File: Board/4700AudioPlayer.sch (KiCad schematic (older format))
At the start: 24 parts, among them U10 74HC74, U11 74HC04, U14 74LS157, U5 74HC40103, U6 74HC40103, U7 74HC40103, U8 74HC40103

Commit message: [RAM] Added new parallel RAM ICs
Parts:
- removed U? (x2): 74HC04, symbol 74xx:74HC04
- removed U?: 74LS10, symbol 74xx:74LS08
- added U? (x2): CY62256-70PC, Package_DIP:DIP-28_W15.24mm, symbol Memory_RAM:CY62256-70PC
- added U? (x8): 74LS393, symbol 74xx:74LS393
- added U?: 74LS157, symbol 74xx:74LS157
- U? (x2): value 74LS10 -> 74LS08
- renumbered U14 to U?
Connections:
- net labels added: ramA_out0, ramA_out1, ramA_out2, ramA_out3, ramA_out4, ramA_out5, ramA_out6, ramA_out7, ramB_out0, ramB_out1, ramB_out2, ramB_out3, ramB_out4, ramB_out5, ramB_out6, ramB_out7
- net labels removed: byte_request, ram_init_cs
- wire segments 347 -> 473
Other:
- moved on the sheet: U11B, U?, U?B

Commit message: [Wave] Added module for played seconds and progress bar. Partially added module for total seconds.
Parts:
- removed U?: 74HC74, symbol 74xx:74HC74
- removed U?: 74HC590, symbol 74xx:74HC590
- added U? (x7): 74HC40103, Package_SO:SOIC-16_3.9x9.9mm_P1.27mm, symbol My_74xx:74HC40103
- added U? (x2): 74LS27, symbol 74xx:74LS27
- added U? (x10): 74LS393, symbol 74xx:74LS393
- added U? (x6): 74LS32, symbol 74xx:74LS32
- added U? (x6): 74LS85, symbol 74xx:74LS85
- added U? (x8): 74HC4511, symbol 74xx:74LS46
- added U?: 74LS154, symbol 74xx:74LS154
- renumbered U to U?
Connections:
- net labels added: reset, sec_clk, sys_clk, total_samples0, total_samples1, total_samples10, total_samples11, total_samples12, total_samples13, total_samples14, total_samples15, total_samples16, total_samples17, total_samples18, total_samples19, total_samples2, total_samples20, total_samples21, total_samples22, total_samples23, total_samples24, total_samples25, total_samples26, total_samples27, total_samples28, total_samples29, total_samples3, total_samples30, total_samples31, total_samples4, total_samples5, total_samples6, total_samples7, total_samples8, total_samples9
- net labels removed: n_ram_clk, n_ram_ready, ram_clk
- wire segments 473 -> 899
- no-connect marks 7 -> 15
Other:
- note added: "16-segment progress bar"
- note added: "Clocks"
- note added: "Header and total sample count determination"
- note added: "Playtime counter"
- note added: "RAMs"
- moved on the sheet: U10A, U11B, U5A, U6A, U7A, U8A, U?, U?A, U?B, U?C

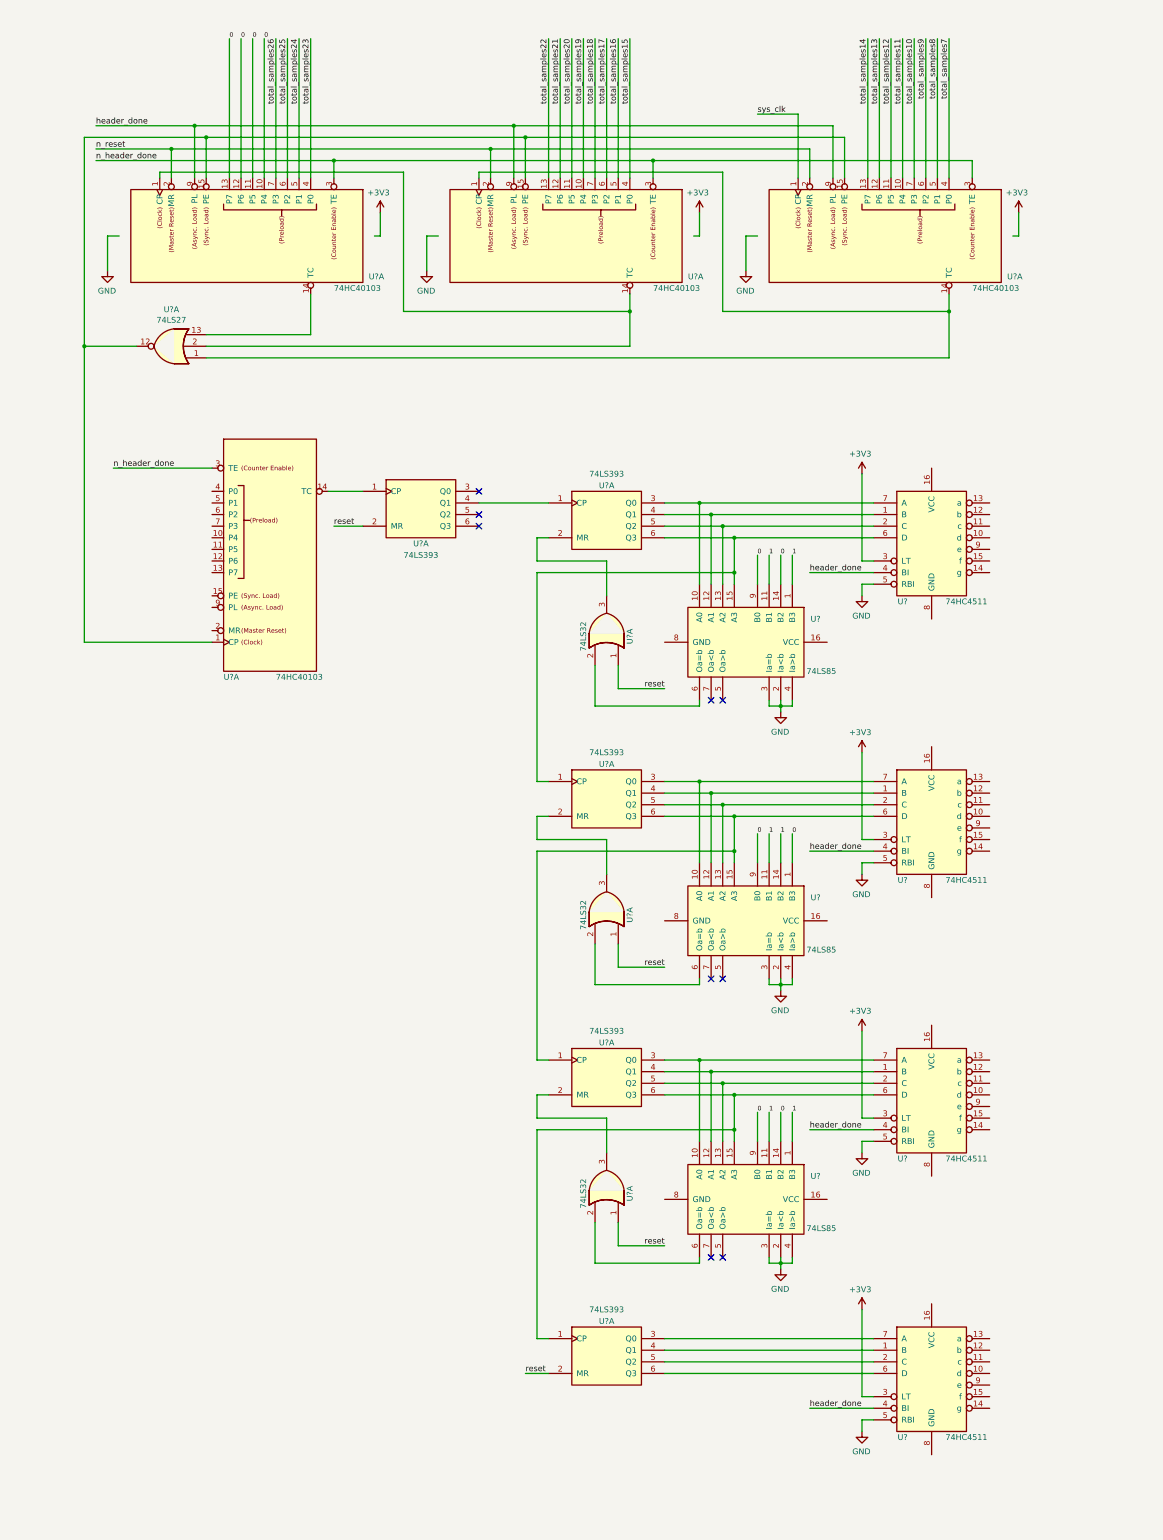
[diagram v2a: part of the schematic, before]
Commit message: [Wave] Fixed calculation of total length
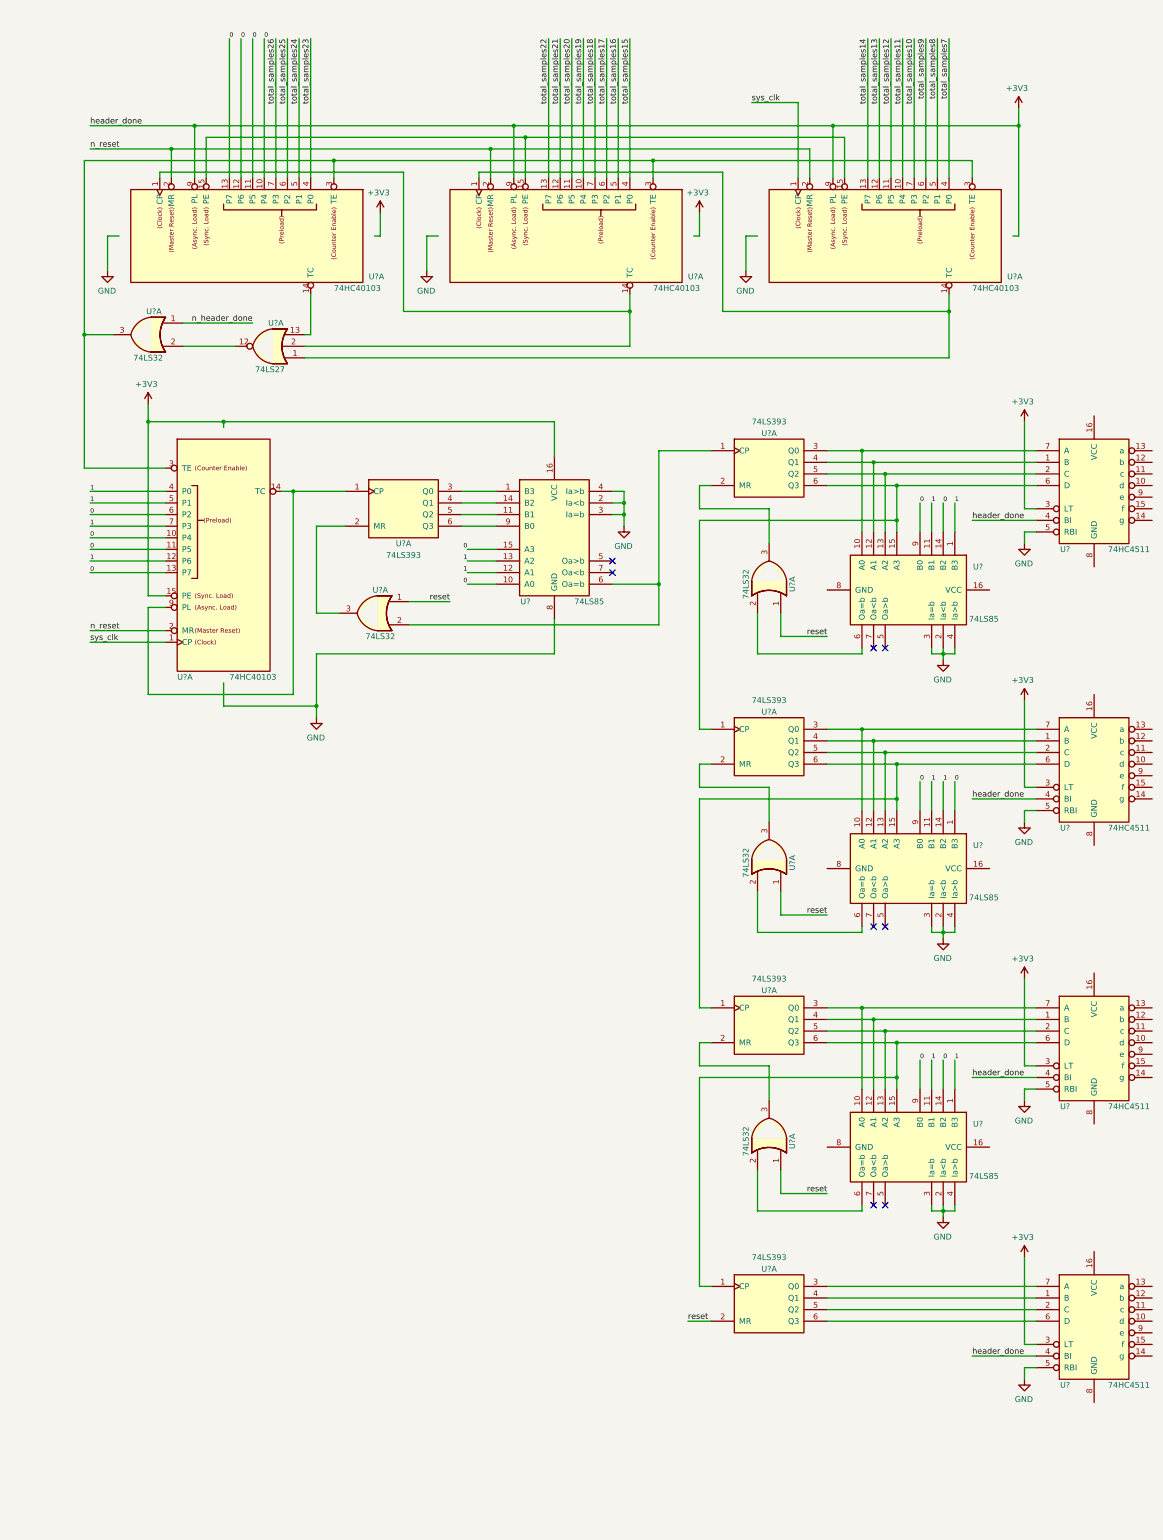
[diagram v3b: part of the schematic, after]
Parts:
- removed U?: 74LS27, symbol 74xx:74LS27
- added U?: 74LS85, symbol 74xx:74LS85
- added U? (x2): 74LS32, symbol 74xx:74LS32
- added U?: 74LS27, symbol 74xx:74LS27
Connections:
- wire segments 899 -> 950
- no-connect marks 15 -> 14
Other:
- moved on the sheet: U?, U?A

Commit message: [Display] Added display RAM
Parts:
- added U? (x32): 74HC151, symbol My_74xx:74HC151
- added U? (x8): 74HC153, symbol My_74xx:74HC153
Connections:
- net labels added: char0_bit0, char0_bit1, char0_bit2, char0_bit3, char0_bit4, char0_bit5, char0_bit6, char0_bit7, char10_bit0, char10_bit1, char10_bit2, char10_bit3, char10_bit4, char10_bit5, char10_bit6, char10_bit7, char11_bit0, char11_bit1, char11_bit2, char11_bit3, char11_bit4, char11_bit5, char11_bit6, char11_bit7, char12_bit0, char12_bit1, char12_bit2, char12_bit3, char12_bit4, char12_bit5, char12_bit6, char12_bit7, char13_bit0, char13_bit1, char13_bit2, char13_bit3, char13_bit4, char13_bit5, char13_bit6, char13_bit7, char14_bit0, char14_bit1, char14_bit2, char14_bit3, char14_bit4, char14_bit5, char14_bit6, char14_bit7, char15_bit0, char15_bit1, char15_bit2, char15_bit3, char15_bit4, char15_bit5, char15_bit6, char15_bit7, char16_bit0, char16_bit1, char16_bit2, char16_bit3, char16_bit4, char16_bit5, char16_bit6, char16_bit7, char17_bit0, char17_bit1, char17_bit2, char17_bit3, char17_bit4, char17_bit5, char17_bit6, char17_bit7, char18_bit0, char18_bit1, char18_bit2, char18_bit3, char18_bit4, char18_bit5, char18_bit6, char18_bit7, char19_bit0, char19_bit1, char19_bit2, char19_bit3, char19_bit4, char19_bit5, char19_bit6, char19_bit7, char1_bit0, char1_bit1, char1_bit2, char1_bit3, char1_bit4, char1_bit5, char1_bit6, char1_bit7, char20_bit0, char20_bit1, char20_bit2, char20_bit3, char20_bit4, char20_bit5, char20_bit6, char20_bit7, char21_bit0, char21_bit1, char21_bit2, char21_bit3, char21_bit4, char21_bit5, char21_bit6, char21_bit7, char22_bit0, char22_bit1, char22_bit2, char22_bit3, char22_bit4, char22_bit5, char22_bit6, char22_bit7, char23_bit0, char23_bit1, char23_bit2, char23_bit3, char23_bit4, char23_bit5, char23_bit6, char23_bit7, char24_bit0, char24_bit1, char24_bit2, char24_bit3, char24_bit4, char24_bit5, char24_bit6, char24_bit7, char25_bit0, char25_bit1, char25_bit2, char25_bit3, char25_bit4, char25_bit5, char25_bit6, char25_bit7, char26_bit0, char26_bit1, char26_bit2, char26_bit3, char26_bit4, char26_bit5, char26_bit6, char26_bit7, char27_bit0, char27_bit1, char27_bit2, char27_bit3, char27_bit4, char27_bit5, char27_bit6, char27_bit7, char28_bit0, char28_bit1, char28_bit2, char28_bit3, char28_bit4, char28_bit5, char28_bit6, char28_bit7, char29_bit0, char29_bit1, char29_bit2, char29_bit3, char29_bit4, char29_bit5, char29_bit6, char29_bit7, char2_bit0, char2_bit1, char2_bit2, char2_bit3, char2_bit4, char2_bit5, char2_bit6, char2_bit7, char30_bit0, char30_bit1, char30_bit2, char30_bit3, char30_bit4, char30_bit5, char30_bit6, char30_bit7, char31_bit0, char31_bit1, char31_bit2, char31_bit3, char31_bit4, char31_bit5, char31_bit6, char31_bit7, char3_bit0, char3_bit1, char3_bit2, char3_bit3, char3_bit4, char3_bit5, char3_bit6, char3_bit7, char4_bit0, char4_bit1, char4_bit2, char4_bit3, char4_bit4, char4_bit5, char4_bit6, char4_bit7, char5_bit0, char5_bit1, char5_bit2, char5_bit3, char5_bit4, char5_bit5, char5_bit6, char5_bit7, char6_bit0, char6_bit1, char6_bit2, char6_bit3, char6_bit4, char6_bit5, char6_bit6, char6_bit7, char7_bit0, char7_bit1, char7_bit2, char7_bit3, char7_bit4, char7_bit5, char7_bit6, char7_bit7, char8_bit0, char8_bit1, char8_bit2, char8_bit3, char8_bit4, char8_bit5, char8_bit6, char8_bit7, char9_bit0, char9_bit1, char9_bit2, char9_bit3, char9_bit4, char9_bit5, char9_bit6, char9_bit7, display_bit0, display_bit1, display_bit2, display_bit3, display_bit4, display_bit5, display_bit6, display_bit7
- wire segments 950 -> 1018
- no-connect marks 14 -> 46

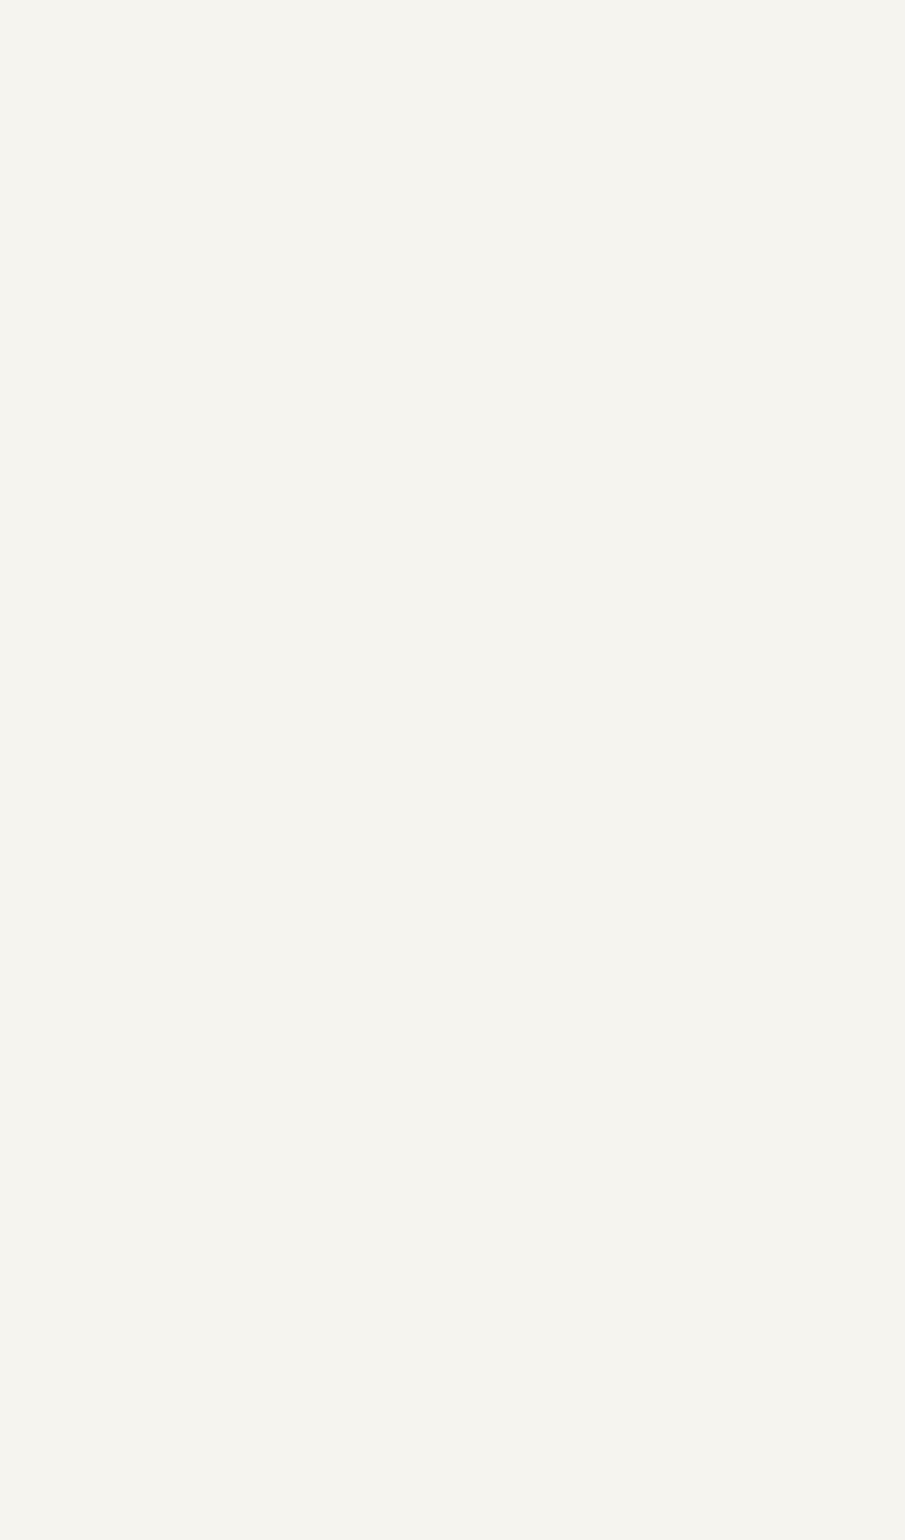
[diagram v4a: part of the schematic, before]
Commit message: [Display] Added signals for display data. Some calculations for RS signal
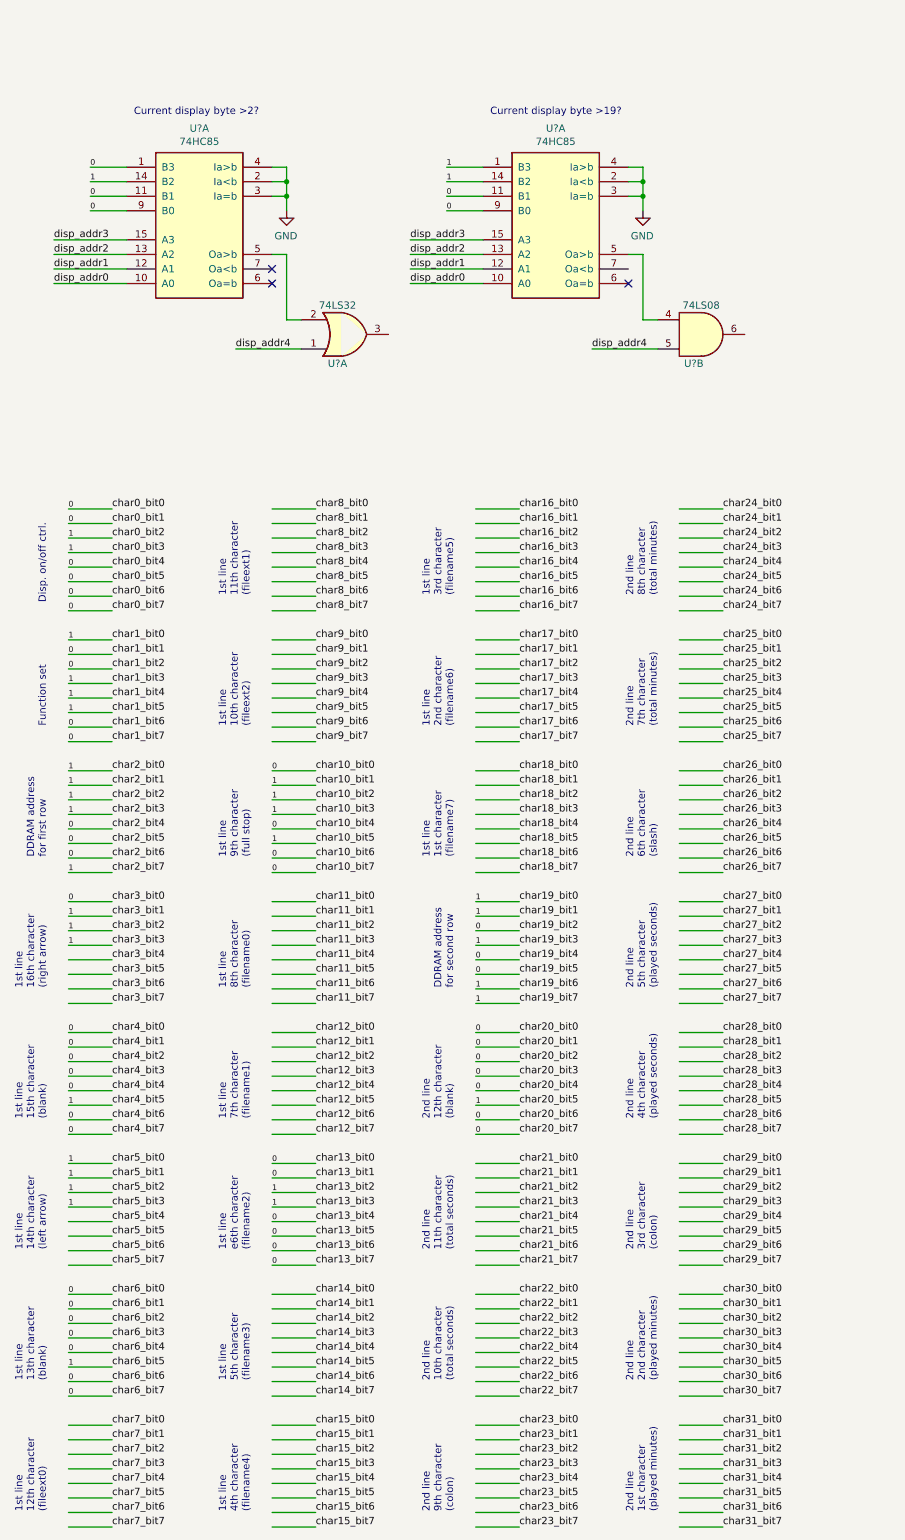
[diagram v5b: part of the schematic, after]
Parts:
- added U? (x2): 74HC85, symbol My_74xx:74HC85
- added U?: 74LS32, symbol 74xx:74LS32
- added U?: 74LS08, symbol 74xx:74LS08
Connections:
- net labels added: disp_addr0, disp_addr1, disp_addr2, disp_addr3, disp_addr4
- wire segments 1018 -> 1310
- no-connect marks 46 -> 49
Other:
- note added: "1st line\n10th character\n(fileext2)"
- note added: "1st line\n11th character\n(fileext1)"
- note added: "1st line\n12th character\n(fileext0)"
- note added: "1st line\n13th character\n(blank)"
- note added: "1st line\n14th character\n(left arrow)"
- note added: "1st line\n15th character\n(blank)"
- note added: "1st line\n16th character\n(right arrow)"
- note added: "1st line\n1st character\n(filename7)"
- note added: "1st line\n2nd character\n(filename6)"
- note added: "1st line\n3rd character\n(filename5)"
- note added: "1st line\n4th character\n(filename4)"
- note added: "1st line\n5th character\n(filename3)"
- note added: "1st line\n7th character\n(filename1)"
- note added: "1st line\n8th character\n(filename0)"
- note added: "1st line\n9th character\n(full stop)"
- note added: "1st line\ne6th character\n(filename2)"
- note added: "2nd line\n10th character\n(total seconds)"
- note added: "2nd line\n11th character\n(total seconds)"
- note added: "2nd line\n12th character\n(blank)"
- note added: "2nd line\n1st character\n(played minutes)"
- note added: "2nd line\n2nd character\n(played minutes)"
- note added: "2nd line\n3rd character\n(colon)"
- note added: "2nd line\n4th character\n(played seconds)"
- note added: "2nd line\n5th character\n(played seconds)"
- note added: "2nd line\n6th character\n(slash)"
- note added: "2nd line\n7th character\n(total minutes)"
- note added: "2nd line\n8th character\n(total minutes)"
- note added: "2nd line\n9th character\n(colon)"
- note added: "Current display byte >19?"
- note added: "Current display byte >2?"
- note added: "DDRAM address\nfor first row"
- note added: "DDRAM address\nfor second row"
- note added: "Disp. on/off ctrl."
- note added: "Function set"

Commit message: [Display] Added circuitry for RS signal.
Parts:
- removed U?: 74HC85, symbol My_74xx:74HC85
- removed U?: 74LS08, symbol 74xx:74LS08
- added U?: 74HC86, symbol 74xx:74HC86
- added U? (x4): 74HC153, symbol My_74xx:74HC153
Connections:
- net labels added: disp_rs
- wire segments 1310 -> 1399
- no-connect marks 49 -> 47
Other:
- note removed: "Current display byte >19?"
- note removed: "Current display byte >2?"
- moved on the sheet: U?A

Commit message: [Board] Moved display stuff to seperate sheet.
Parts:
- removed U?: 74HC86, symbol 74xx:74HC86
- removed U? (x32): 74HC151, symbol My_74xx:74HC151
- removed U? (x12): 74HC153, symbol My_74xx:74HC153
- removed U?: 74HC85, symbol My_74xx:74HC85
- removed U?: 74LS32, symbol 74xx:74LS32
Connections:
- net labels removed: char0_bit0, char0_bit1, char0_bit2, char0_bit3, char0_bit4, char0_bit5, char0_bit6, char0_bit7, char10_bit0, char10_bit1, char10_bit2, char10_bit3, char10_bit4, char10_bit5, char10_bit6, char10_bit7, char11_bit0, char11_bit1, char11_bit2, char11_bit3, char11_bit4, char11_bit5, char11_bit6, char11_bit7, char12_bit0, char12_bit1, char12_bit2, char12_bit3, char12_bit4, char12_bit5, char12_bit6, char12_bit7, char13_bit0, char13_bit1, char13_bit2, char13_bit3, char13_bit4, char13_bit5, char13_bit6, char13_bit7, char14_bit0, char14_bit1, char14_bit2, char14_bit3, char14_bit4, char14_bit5, char14_bit6, char14_bit7, char15_bit0, char15_bit1, char15_bit2, char15_bit3, char15_bit4, char15_bit5, char15_bit6, char15_bit7, char16_bit0, char16_bit1, char16_bit2, char16_bit3, char16_bit4, char16_bit5, char16_bit6, char16_bit7, char17_bit0, char17_bit1, char17_bit2, char17_bit3, char17_bit4, char17_bit5, char17_bit6, char17_bit7, char18_bit0, char18_bit1, char18_bit2, char18_bit3, char18_bit4, char18_bit5, char18_bit6, char18_bit7, char19_bit0, char19_bit1, char19_bit2, char19_bit3, char19_bit4, char19_bit5, char19_bit6, char19_bit7, char1_bit0, char1_bit1, char1_bit2, char1_bit3, char1_bit4, char1_bit5, char1_bit6, char1_bit7, char20_bit0, char20_bit1, char20_bit2, char20_bit3, char20_bit4, char20_bit5, char20_bit6, char20_bit7, char21_bit0, char21_bit1, char21_bit2, char21_bit3, char21_bit4, char21_bit5, char21_bit6, char21_bit7, char22_bit0, char22_bit1, char22_bit2, char22_bit3, char22_bit4, char22_bit5, char22_bit6, char22_bit7, char23_bit0, char23_bit1, char23_bit2, char23_bit3, char23_bit4, char23_bit5, char23_bit6, char23_bit7, char24_bit0, char24_bit1, char24_bit2, char24_bit3, char24_bit4, char24_bit5, char24_bit6, char24_bit7, char25_bit0, char25_bit1, char25_bit2, char25_bit3, char25_bit4, char25_bit5, char25_bit6, char25_bit7, char26_bit0, char26_bit1, char26_bit2, char26_bit3, char26_bit4, char26_bit5, char26_bit6, char26_bit7, char27_bit0, char27_bit1, char27_bit2, char27_bit3, char27_bit4, char27_bit5, char27_bit6, char27_bit7, char28_bit0, char28_bit1, char28_bit2, char28_bit3, char28_bit4, char28_bit5, char28_bit6, char28_bit7, char29_bit0, char29_bit1, char29_bit2, char29_bit3, char29_bit4, char29_bit5, char29_bit6, char29_bit7, char2_bit0, char2_bit1, char2_bit2, char2_bit3, char2_bit4, char2_bit5, char2_bit6, char2_bit7, char30_bit0, char30_bit1, char30_bit2, char30_bit3, char30_bit4, char30_bit5, char30_bit6, char30_bit7, char31_bit0, char31_bit1, char31_bit2, char31_bit3, char31_bit4, char31_bit5, char31_bit6, char31_bit7, char3_bit0, char3_bit1, char3_bit2, char3_bit3, char3_bit4, char3_bit5, char3_bit6, char3_bit7, char4_bit0, char4_bit1, char4_bit2, char4_bit3, char4_bit4, char4_bit5, char4_bit6, char4_bit7, char5_bit0, char5_bit1, char5_bit2, char5_bit3, char5_bit4, char5_bit5, char5_bit6, char5_bit7, char6_bit0, char6_bit1, char6_bit2, char6_bit3, char6_bit4, char6_bit5, char6_bit6, char6_bit7, char7_bit0, char7_bit1, char7_bit2, char7_bit3, char7_bit4, char7_bit5, char7_bit6, char7_bit7, char8_bit0, char8_bit1, char8_bit2, char8_bit3, char8_bit4, char8_bit5, char8_bit6, char8_bit7, char9_bit0, char9_bit1, char9_bit2, char9_bit3, char9_bit4, char9_bit5, char9_bit6, char9_bit7, disp_addr0, disp_addr1, disp_addr2, disp_addr3, disp_addr4, disp_rs, display_bit0, display_bit1, display_bit2, display_bit3, display_bit4, display_bit5, display_bit6, display_bit7
- wire segments 1399 -> 890
- no-connect marks 47 -> 14
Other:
- note removed: "1st line\n10th character\n(fileext2)"
- note removed: "1st line\n11th character\n(fileext1)"
- note removed: "1st line\n12th character\n(fileext0)"
- note removed: "1st line\n13th character\n(blank)"
- note removed: "1st line\n14th character\n(left arrow)"
- note removed: "1st line\n15th character\n(blank)"
- note removed: "1st line\n16th character\n(right arrow)"
- note removed: "1st line\n1st character\n(filename7)"
- note removed: "1st line\n2nd character\n(filename6)"
- note removed: "1st line\n3rd character\n(filename5)"
- note removed: "1st line\n4th character\n(filename4)"
- note removed: "1st line\n5th character\n(filename3)"
- note removed: "1st line\n7th character\n(filename1)"
- note removed: "1st line\n8th character\n(filename0)"
- note removed: "1st line\n9th character\n(full stop)"
- note removed: "1st line\ne6th character\n(filename2)"
- note removed: "2nd line\n10th character\n(total seconds)"
- note removed: "2nd line\n11th character\n(total seconds)"
- note removed: "2nd line\n12th character\n(blank)"
- note removed: "2nd line\n1st character\n(played minutes)"
- note removed: "2nd line\n2nd character\n(played minutes)"
- note removed: "2nd line\n3rd character\n(colon)"
- note removed: "2nd line\n4th character\n(played seconds)"
- note removed: "2nd line\n5th character\n(played seconds)"
- note removed: "2nd line\n6th character\n(slash)"
- note removed: "2nd line\n7th character\n(total minutes)"
- note removed: "2nd line\n8th character\n(total minutes)"
- note removed: "2nd line\n9th character\n(colon)"
- note removed: "DDRAM address\nfor first row"
- note removed: "DDRAM address\nfor second row"
- note removed: "Disp. on/off ctrl."
- note removed: "Function set"

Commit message: [Board] Moved all other pieces into seperate hierarchical sheets.
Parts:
- removed U10: 74HC74, symbol 74xx:74HC74
- removed U11: 74HC04, symbol 74xx:74HC04
- removed U5, U6, U7, U8, U? (x8): 74HC40103, Package_SO:SOIC-16_3.9x9.9mm_P1.27mm, symbol My_74xx:74HC40103
- removed U? (x9): 74LS32, symbol 74xx:74LS32
- removed U? (x2): 74LS08, symbol 74xx:74LS08
- removed U? (x2): 74LS157, symbol 74xx:74LS157
- removed U? (x5): 74LS574, symbol 74xx:74LS574
- removed U? (x18): 74LS393, symbol 74xx:74LS393
- removed U?: 4072, symbol 4xxx:4072
- removed U? (x2): 74LS10, symbol 74xx:74LS10
- removed U? (x7): 74LS85, symbol 74xx:74LS85
- removed U? (x8): 74HC4511, symbol 74xx:74LS46
- removed U? (x2): CY62256-70PC, Package_DIP:DIP-28_W15.24mm, symbol Memory_RAM:CY62256-70PC
- removed U? (x2): 74LS27, symbol 74xx:74LS27
- removed U?: 74LS154, symbol 74xx:74LS154
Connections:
- no-connect marks 14 -> 0
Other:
- note removed: "16-segment progress bar"
- note removed: "Clocks"
- note removed: "Header and total sample count determination"
- note removed: "Playtime counter"
- note removed: "RAMs"
